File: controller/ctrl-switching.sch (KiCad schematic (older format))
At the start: 42 parts, among them J25 INDICATION1, J26 INDICATION2, U10 ULN2803A, U11 ULN2803A, U9 74HC595

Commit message: Change gas pedal interface so that it supports going up and down from the middle voltage so that it's compatible with Linde forklift gas mechanism
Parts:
- D35, D36, D37, D38, D39, D40, D41, D42, D43, D44, D45, D46, D47, D48, D49, D50: footprint (none) -> LEDs:LED_0805
- R23, R24, R25, R26, R27, R28, R29, R30, R31, R32, R33, R34, R35, R36, R37, R38, R39, R40, R41: footprint (none) -> Resistors_SMD:R_0603_HandSoldering
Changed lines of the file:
@@
 GAZ_SPEED1
 $Comp
-L GND #PWR013
+L GND #PWR18
 U 1 1 58CDDCEF
 P 7850 4800
-F 0 "#PWR013" H 4700 1700 50  0001 C CNN
+F 0 "#PWR18" H 4700 1700 50  0001 C CNN
 F 1 "GND" H 7855 4627 50  0000 C CNN
 F 2 "" H 4700 1950 50  0001 C CNN
@@
 $EndComp
 $Comp
-L GND #PWR014
+L GND #PWR19
 U 1 1 58CDDD09
 P 7950 9350
-F 0 "#PWR014" H 4800 6250 50  0001 C CNN
+F 0 "#PWR19" H 4800 6250 50  0001 C CNN
 F 1 "GND" H 7955 9177 50  0000 C CNN
 F 2 "" H 4800 6500 50  0001 C CNN
@@
 $EndComp
 $Comp
-L GND #PWR015
+L GND #PWR17
 U 1 1 58CDDF2F
 P 7400 9850
-F 0 "#PWR015" H 4250 6750 50  0001 C CNN
+F 0 "#PWR17" H 4250 6750 50  0001 C CNN
 F 1 "GND" H 7405 9677 50  0000 C CNN
 F 2 "" H 4250 7000 50  0001 C CNN
@@
 $EndComp
 $Comp
-L GND #PWR016
+L GND #PWR16
 U 1 1 58CDE24D
 P 7250 5300
-F 0 "#PWR016" H 4100 2200 50  0001 C CNN
+F 0 "#PWR16" H 4100 2200 50  0001 C CNN
 F 1 "GND" H 7255 5127 50  0000 C CNN
 F 2 "" H 4100 2450 50  0001 C CNN
@@
 DATA
 $Comp
-L +5V #PWR017
+L +5V #PWR14
 U 1 1 58CF6852
 P 4950 8050
-F 0 "#PWR017" H 1550 3750 50  0001 C CNN
+F 0 "#PWR14" H 1550 3750 50  0001 C CNN
 F 1 "+5V" H 4965 8223 50  0000 C CNN
 F 2 "" H 1550 3900 50  0001 C CNN
@@
 $EndComp
 $Comp
-L GND #PWR018
+L GND #PWR15
 U 1 1 58CF68A7
 P 5100 8950
-F 0 "#PWR018" H 1950 5850 50  0001 C CNN
+F 0 "#PWR15" H 1950 5850 50  0001 C CNN
 F 1 "GND" H 5105 8777 50  0000 C CNN
 F 2 "" H 1950 6100 50  0001 C CNN
@@
 F 0 "R23" V 4343 8350 50  0000 C CNN
 F 1 "R" V 4434 8350 50  0000 C CNN
-F 2 "" V 1730 4150 50  0001 C CNN
+F 2 "Resistors_SMD:R_0603_HandSoldering" V 1730 4150 50  0001 C CNN
 F 3 "" H 1800 4150 50  0001 C CNN
 	1    4550 8350
@@
 F 0 "R24" V 4343 8550 50  0000 C CNN
 F 1 "R" V 4434 8550 50  0000 C CNN
-F 2 "" V 1730 4350 50  0001 C CNN
+F 2 "Resistors_SMD:R_0603_HandSoldering" V 1730 4350 50  0001 C CNN
 F 3 "" H 1800 4350 50  0001 C CNN
 	1    4550 8550
@@
 F 0 "R25" V 4343 8850 50  0000 C CNN
 F 1 "R" V 4434 8850 50  0000 C CNN
-F 2 "" V 1730 4650 50  0001 C CNN
+F 2 "Resistors_SMD:R_0603_HandSoldering" V 1730 4650 50  0001 C CNN
 F 3 "" H 1800 4650 50  0001 C CNN
 	1    4550 8850
@@
 F 0 "D39" H 9400 2900 50  0000 C CNN
 F 1 "LED_Small_ALT" H 9400 2944 50  0001 C CNN
-F 2 "" V 1250 1700 50  0001 C CNN
+F 2 "LEDs:LED_0805" V 1250 1700 50  0001 C CNN
 F 3 "" V 1250 1700 50  0001 C CNN
 	1    9400 2800
@@
 F 0 "R30" V 9550 2800 50  0000 C CNN
 F 1 "R" V 9650 2800 50  0000 C CNN
-F 2 "" V 6830 -1400 50  0001 C CNN
+F 2 "Resistors_SMD:R_0603_HandSoldering" V 6830 -1400 50  0001 C CNN
 F 3 "" H 6900 -1400 50  0001 C CNN
 	1    9650 2800
@@
 F 0 "D40" H 9400 3100 50  0000 C CNN
 F 1 "LED_Small_ALT" H 9400 3144 50  0001 C CNN
-F 2 "" V 1250 1900 50  0001 C CNN
+F 2 "LEDs:LED_0805" V 1250 1900 50  0001 C CNN
 F 3 "" V 1250 1900 50  0001 C CNN
 	1    9400 3000
@@
 F 0 "R31" V 9550 3000 50  0000 C CNN
 F 1 "R" V 9650 3000 50  0000 C CNN
-F 2 "" V 6830 -1200 50  0001 C CNN
+F 2 "Resistors_SMD:R_0603_HandSoldering" V 6830 -1200 50  0001 C CNN
 F 3 "" H 6900 -1200 50  0001 C CNN
 	1    9650 3000
@@
 F 0 "D41" H 9400 3300 50  0000 C CNN
 F 1 "LED_Small_ALT" H 9400 3344 50  0001 C CNN
-F 2 "" V 1250 2100 50  0001 C CNN
+F 2 "LEDs:LED_0805" V 1250 2100 50  0001 C CNN
 F 3 "" V 1250 2100 50  0001 C CNN
 	1    9400 3200
@@
 F 0 "R32" V 9550 3200 50  0000 C CNN
 F 1 "R" V 9650 3200 50  0000 C CNN
-F 2 "" V 6830 -1000 50  0001 C CNN
+F 2 "Resistors_SMD:R_0603_HandSoldering" V 6830 -1000 50  0001 C CNN
 F 3 "" H 6900 -1000 50  0001 C CNN
 	1    9650 3200
@@
 F 0 "D42" H 9400 3500 50  0000 C CNN
 F 1 "LED_Small_ALT" H 9400 3544 50  0001 C CNN
-F 2 "" V 1250 2300 50  0001 C CNN
+F 2 "LEDs:LED_0805" V 1250 2300 50  0001 C CNN
 F 3 "" V 1250 2300 50  0001 C CNN
 	1    9400 3400
@@
 F 0 "R33" V 9550 3400 50  0000 C CNN
 F 1 "R" V 9650 3400 50  0000 C CNN
-F 2 "" V 6830 -800 50  0001 C CNN
+F 2 "Resistors_SMD:R_0603_HandSoldering" V 6830 -800 50  0001 C CNN
 F 3 "" H 6900 -800 50  0001 C CNN
 	1    9650 3400
@@
 F 0 "D35" H 9400 2100 50  0000 C CNN
 F 1 "LED_Small_ALT" H 9400 2144 50  0001 C CNN
-F 2 "" V 1250 900 50  0001 C CNN
+F 2 "LEDs:LED_0805" V 1250 900 50  0001 C CNN
 F 3 "" V 1250 900 50  0001 C CNN
 	1    9400 2000
@@
 F 0 "R26" V 9550 2000 50  0000 C CNN
 F 1 "R" V 9650 2000 50  0000 C CNN
-F 2 "" V 6830 -2200 50  0001 C CNN
+F 2 "Resistors_SMD:R_0603_HandSoldering" V 6830 -2200 50  0001 C CNN
 F 3 "" H 6900 -2200 50  0001 C CNN
 	1    9650 2000
@@
 F 0 "D36" H 9400 2300 50  0000 C CNN
 F 1 "LED_Small_ALT" H 9400 2344 50  0001 C CNN
-F 2 "" V 1250 1100 50  0001 C CNN
+F 2 "LEDs:LED_0805" V 1250 1100 50  0001 C CNN
 F 3 "" V 1250 1100 50  0001 C CNN
 	1    9400 2200
@@
 F 0 "R27" V 9550 2200 50  0000 C CNN
 F 1 "R" V 9650 2200 50  0000 C CNN
-F 2 "" V 6830 -2000 50  0001 C CNN
+F 2 "Resistors_SMD:R_0603_HandSoldering" V 6830 -2000 50  0001 C CNN
 F 3 "" H 6900 -2000 50  0001 C CNN
 	1    9650 2200
@@
 F 0 "D37" H 9400 2500 50  0000 C CNN
 F 1 "LED_Small_ALT" H 9400 2544 50  0001 C CNN
-F 2 "" V 1250 1300 50  0001 C CNN
+F 2 "LEDs:LED_0805" V 1250 1300 50  0001 C CNN
 F 3 "" V 1250 1300 50  0001 C CNN
 	1    9400 2400
@@
 F 0 "R28" V 9550 2400 50  0000 C CNN
 F 1 "R" V 9650 2400 50  0000 C CNN
-F 2 "" V 6830 -1800 50  0001 C CNN
+F 2 "Resistors_SMD:R_0603_HandSoldering" V 6830 -1800 50  0001 C CNN
 F 3 "" H 6900 -1800 50  0001 C CNN
 	1    9650 2400
@@
 F 0 "D38" H 9400 2700 50  0000 C CNN
 F 1 "LED_Small_ALT" H 9400 2744 50  0001 C CNN
-F 2 "" V 1250 1500 50  0001 C CNN
+F 2 "LEDs:LED_0805" V 1250 1500 50  0001 C CNN
 F 3 "" V 1250 1500 50  0001 C CNN
 	1    9400 2600
@@
 F 0 "R29" V 9550 2600 50  0000 C CNN
 F 1 "R" V 9650 2600 50  0000 C CNN
-F 2 "" V 6830 -1600 50  0001 C CNN
+F 2 "Resistors_SMD:R_0603_HandSoldering" V 6830 -1600 50  0001 C CNN
 F 3 "" H 6900 -1600 50  0001 C CNN
 	1    9650 2600
@@
 F 0 "D47" H 9500 7450 50  0000 C CNN
 F 1 "LED_Small_ALT" H 9500 7494 50  0001 C CNN
-F 2 "" V 1350 6250 50  0001 C CNN
+F 2 "LEDs:LED_0805" V 1350 6250 50  0001 C CNN
 F 3 "" V 1350 6250 50  0001 C CNN
 	1    9500 7350
@@
 F 0 "R38" V 9650 7350 50  0000 C CNN
 F 1 "R" V 9750 7350 50  0000 C CNN
-F 2 "" V 6930 3150 50  0001 C CNN
+F 2 "Resistors_SMD:R_0603_HandSoldering" V 6930 3150 50  0001 C CNN
 F 3 "" H 7000 3150 50  0001 C CNN
 	1    9750 7350
@@
 F 0 "D48" H 9500 7650 50  0000 C CNN
 F 1 "LED_Small_ALT" H 9500 7694 50  0001 C CNN
-F 2 "" V 1350 6450 50  0001 C CNN
+F 2 "LEDs:LED_0805" V 1350 6450 50  0001 C CNN
 F 3 "" V 1350 6450 50  0001 C CNN
 	1    9500 7550
@@
 F 0 "R39" V 9650 7550 50  0000 C CNN
 F 1 "R" V 9750 7550 50  0000 C CNN
-F 2 "" V 6930 3350 50  0001 C CNN
+F 2 "Resistors_SMD:R_0603_HandSoldering" V 6930 3350 50  0001 C CNN
 F 3 "" H 7000 3350 50  0001 C CNN
 	1    9750 7550
@@
 F 0 "D49" H 9500 7850 50  0000 C CNN
 F 1 "LED_Small_ALT" H 9500 7894 50  0001 C CNN
-F 2 "" V 1350 6650 50  0001 C CNN
+F 2 "LEDs:LED_0805" V 1350 6650 50  0001 C CNN
 F 3 "" V 1350 6650 50  0001 C CNN
 	1    9500 7750
@@
 F 0 "R40" V 9650 7750 50  0000 C CNN
 F 1 "R" V 9750 7750 50  0000 C CNN
-F 2 "" V 6930 3550 50  0001 C CNN
+F 2 "Resistors_SMD:R_0603_HandSoldering" V 6930 3550 50  0001 C CNN
 F 3 "" H 7000 3550 50  0001 C CNN
 	1    9750 7750
@@
 F 0 "D50" H 9500 8050 50  0000 C CNN
 F 1 "LED_Small_ALT" H 9500 8094 50  0001 C CNN
-F 2 "" V 1350 6850 50  0001 C CNN
+F 2 "LEDs:LED_0805" V 1350 6850 50  0001 C CNN
 F 3 "" V 1350 6850 50  0001 C CNN
 	1    9500 7950
@@
 F 0 "R41" V 9650 7950 50  0000 C CNN
 F 1 "R" V 9750 7950 50  0000 C CNN
-F 2 "" V 6930 3750 50  0001 C CNN
+F 2 "Resistors_SMD:R_0603_HandSoldering" V 6930 3750 50  0001 C CNN
 F 3 "" H 7000 3750 50  0001 C CNN
 	1    9750 7950
@@
 F 0 "D43" H 9500 6650 50  0000 C CNN
 F 1 "LED_Small_ALT" H 9500 6694 50  0001 C CNN
-F 2 "" V 1350 5450 50  0001 C CNN
+F 2 "LEDs:LED_0805" V 1350 5450 50  0001 C CNN
 F 3 "" V 1350 5450 50  0001 C CNN
 	1    9500 6550
@@
 F 0 "R34" V 9650 6550 50  0000 C CNN
 F 1 "R" V 9750 6550 50  0000 C CNN
-F 2 "" V 6930 2350 50  0001 C CNN
+F 2 "Resistors_SMD:R_0603_HandSoldering" V 6930 2350 50  0001 C CNN
 F 3 "" H 7000 2350 50  0001 C CNN
 	1    9750 6550
@@
 F 0 "D44" H 9500 6850 50  0000 C CNN
 F 1 "LED_Small_ALT" H 9500 6894 50  0001 C CNN
-F 2 "" V 1350 5650 50  0001 C CNN
+F 2 "LEDs:LED_0805" V 1350 5650 50  0001 C CNN
 F 3 "" V 1350 5650 50  0001 C CNN
 	1    9500 6750
@@
 F 0 "R35" V 9650 6750 50  0000 C CNN
 F 1 "R" V 9750 6750 50  0000 C CNN
-F 2 "" V 6930 2550 50  0001 C CNN
+F 2 "Resistors_SMD:R_0603_HandSoldering" V 6930 2550 50  0001 C CNN
 F 3 "" H 7000 2550 50  0001 C CNN
 	1    9750 6750
@@
 F 0 "D45" H 9500 7050 50  0000 C CNN
 F 1 "LED_Small_ALT" H 9500 7094 50  0001 C CNN
-F 2 "" V 1350 5850 50  0001 C CNN
+F 2 "LEDs:LED_0805" V 1350 5850 50  0001 C CNN
 F 3 "" V 1350 5850 50  0001 C CNN
 	1    9500 6950
@@
 F 0 "R36" V 9650 6950 50  0000 C CNN
 F 1 "R" V 9750 6950 50  0000 C CNN
-F 2 "" V 6930 2750 50  0001 C CNN
+F 2 "Resistors_SMD:R_0603_HandSoldering" V 6930 2750 50  0001 C CNN
 F 3 "" H 7000 2750 50  0001 C CNN
 	1    9750 6950
@@
 F 0 "D46" H 9500 7250 50  0000 C CNN
 F 1 "LED_Small_ALT" H 9500 7294 50  0001 C CNN
-F 2 "" V 1350 6050 50  0001 C CNN
+F 2 "LEDs:LED_0805" V 1350 6050 50  0001 C CNN
 F 3 "" V 1350 6050 50  0001 C CNN
 	1    9500 7150
@@
 F 0 "R37" V 9650 7150 50  0000 C CNN
 F 1 "R" V 9750 7150 50  0000 C CNN
-F 2 "" V 6930 2950 50  0001 C CNN
+F 2 "Resistors_SMD:R_0603_HandSoldering" V 6930 2950 50  0001 C CNN
 F 3 "" H 7000 2950 50  0001 C CNN
 	1    9750 7150

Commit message: More or less final controller board
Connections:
- net labels added: GAZ_SPEED3, ~GAZ_SPEED3_PWR

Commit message: Some progress with controller board routing
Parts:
- removed RN2: R_Network08, Resistors_THT:R_Array_SIP9, symbol R_Network08
- added RN2: R_Pack08, Resistors_SMD:R_Array_Convex_8x0602, symbol R_Pack08
- D35, D36, D37, D38, D39, D40, D41, D42, D45, D48, D49, D50: footprint LEDs:LED_0805 -> LEDs:LED_D5.0mm; Distributor (none) -> ?; Manufacturer (none) -> ?; PartNo (none) -> ?
- D43: renamed from D47; footprint LEDs:LED_0805 -> LEDs:LED_D5.0mm; Distributor (none) -> ?; Manufacturer (none) -> ?; PartNo (none) -> ?
- D44: renamed from D46; footprint LEDs:LED_0805 -> LEDs:LED_D5.0mm; Distributor (none) -> ?; Manufacturer (none) -> ?; PartNo (none) -> ?
- D46: renamed from D44; footprint LEDs:LED_0805 -> LEDs:LED_D5.0mm; Distributor (none) -> ?; Manufacturer (none) -> ?; PartNo (none) -> ?
- D47: renamed from D43; footprint LEDs:LED_0805 -> LEDs:LED_D5.0mm; Distributor (none) -> ?; Manufacturer (none) -> ?; PartNo (none) -> ?
- U9: footprint (none) -> Housings_SOIC:SOIC-16_3.9x9.9mm_Pitch1.27mm; Distributor (none) -> ?; Manufacturer (none) -> ?; PartNo (none) -> ?
- renumbered R38 to R34, R37 to R35, R35 to R37, R34 to R38
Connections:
- wire segments 96 -> 97

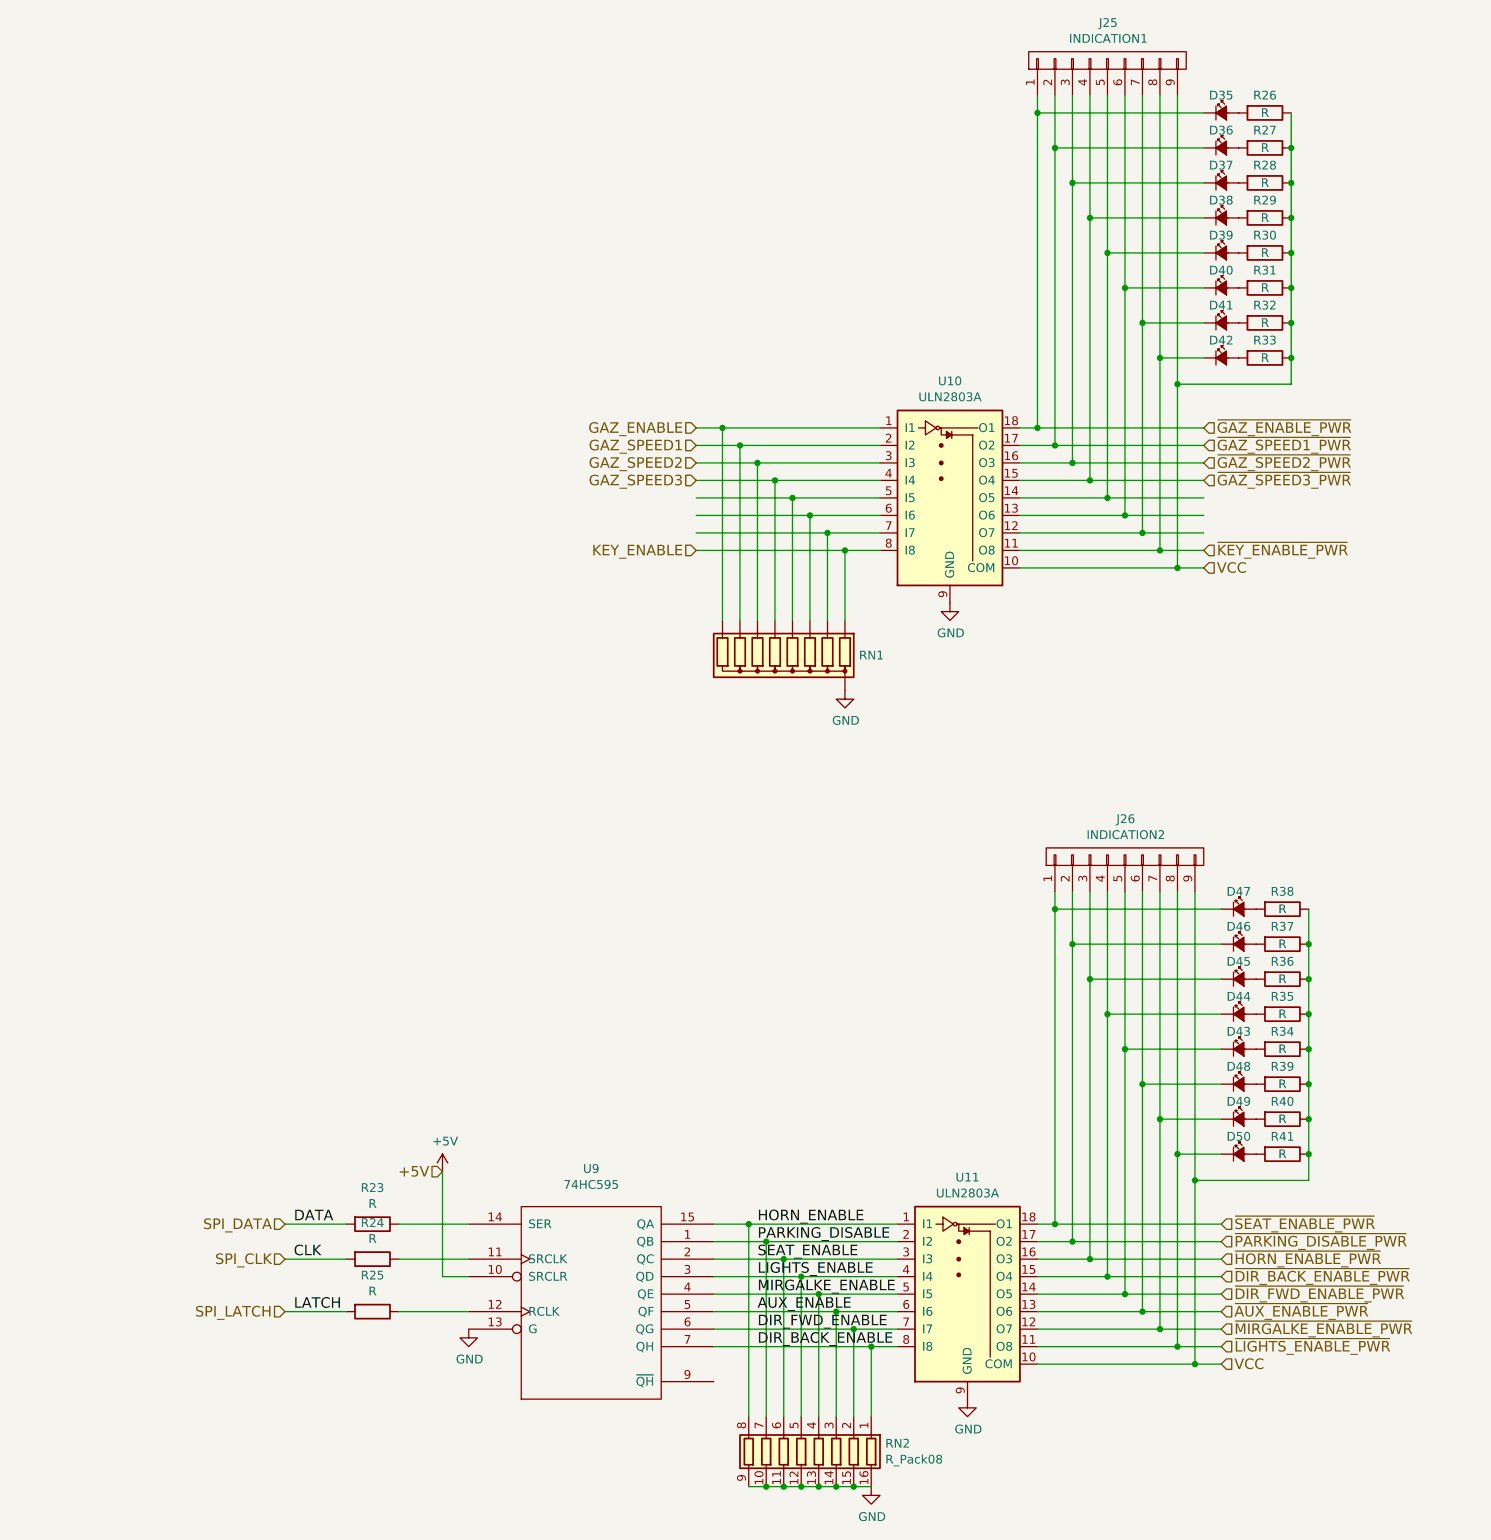
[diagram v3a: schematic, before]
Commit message: Finish the routing, add some significant fixes: *correct to-252 pin numbering * longer pads for relays * fix footprint of the optocouplers
Also finish the routing
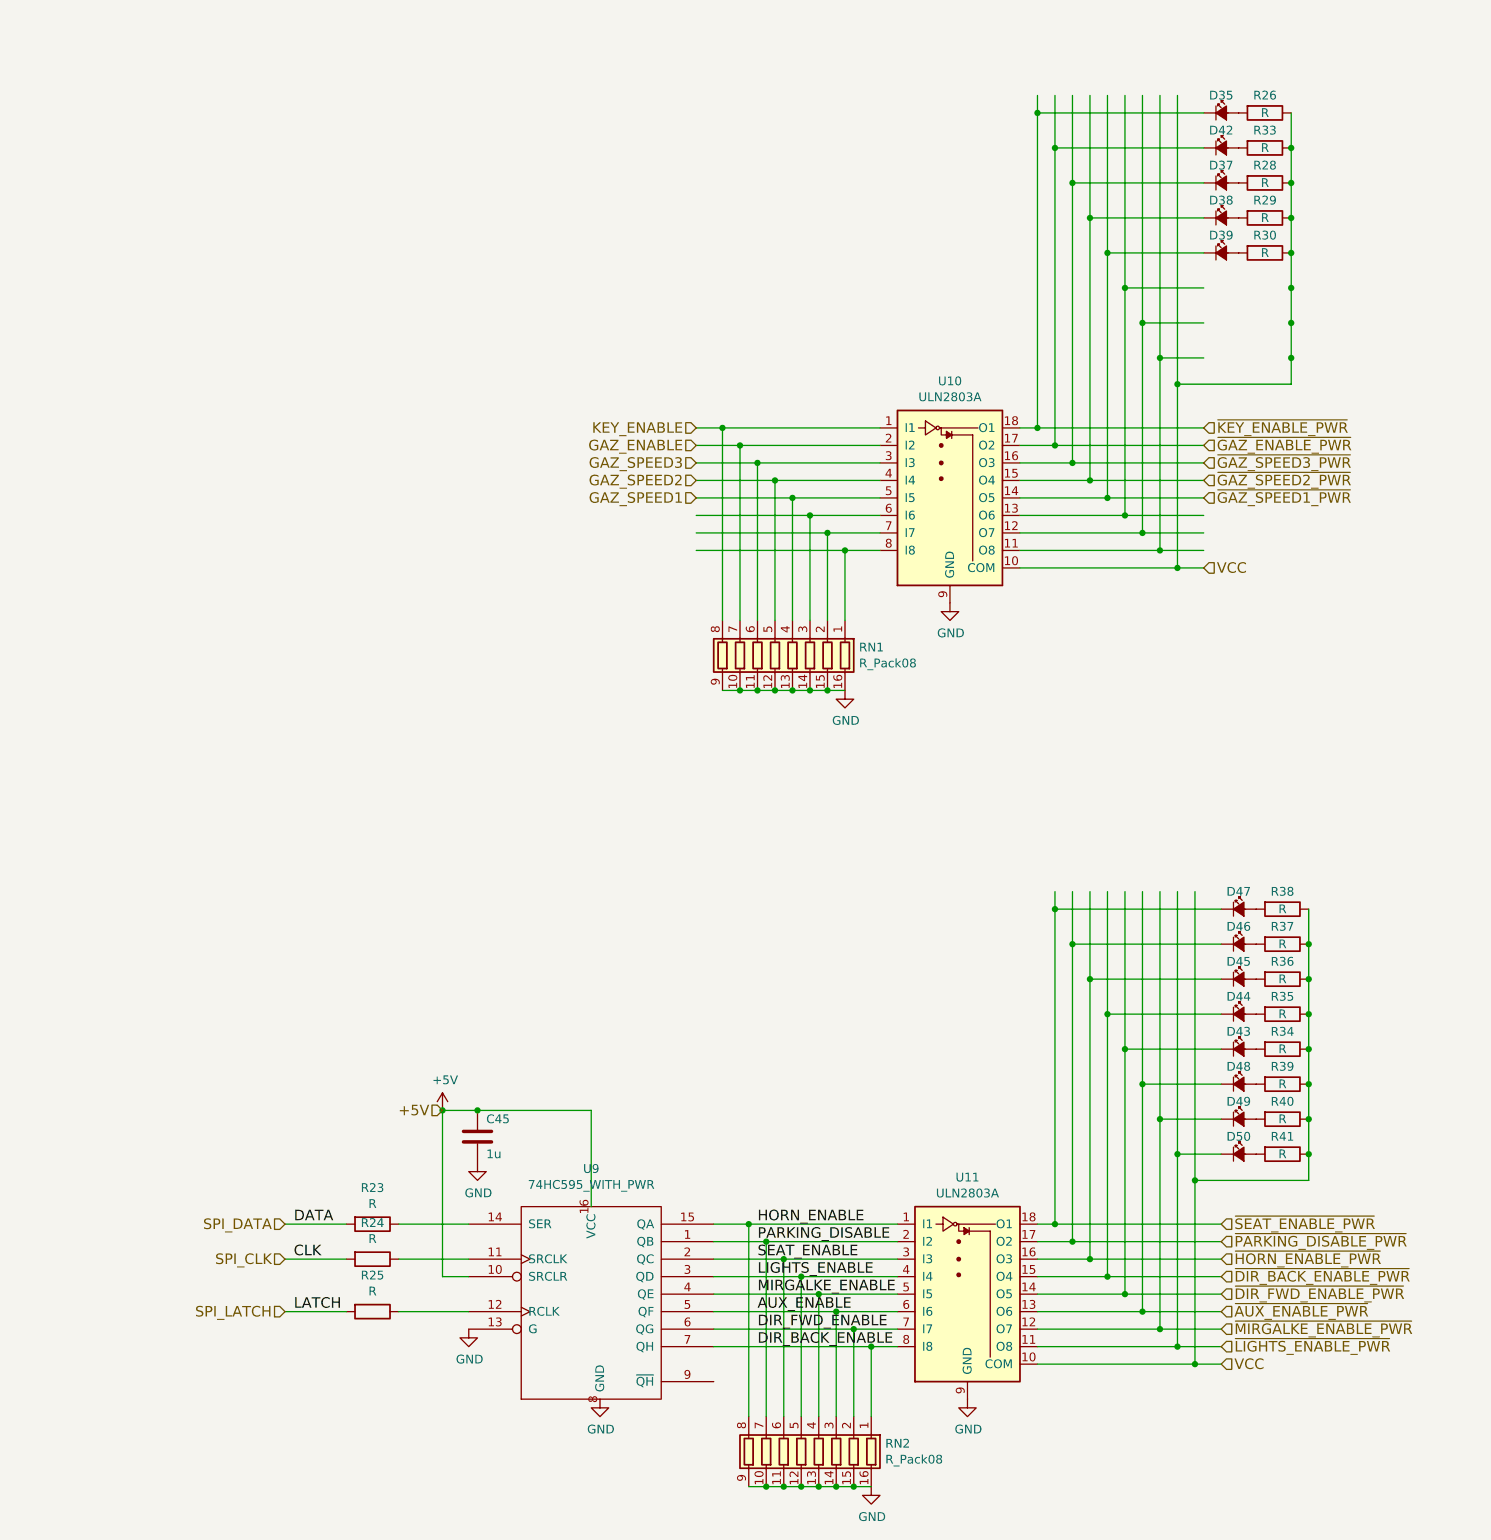
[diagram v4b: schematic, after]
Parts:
- removed D36, D40, D41: LED_Small_ALT, LEDs:LED_D5.0mm, symbol LED_Small_ALT
- removed J25: INDICATION1, symbol CONN_01X09
- removed J26: INDICATION2, symbol CONN_01X09
- removed R27, R31, R32: R, Resistors_SMD:R_0603_HandSoldering, symbol R
- removed RN1: R_Network08, Resistors_THT:R_Array_SIP9, symbol R_Network08
- removed U9: 74HC595, Housings_SOIC:SOIC-16_3.9x9.9mm_Pitch1.27mm, symbol 74HC595
- added C45: 1u, Capacitors_SMD:C_0603_HandSoldering, symbol C
- added RN1: R_Pack08, Resistors_SMD:R_Array_Convex_8x0602, symbol R_Pack08
- added U9: 74HC595_WITH_PWR, Housings_SOIC:SOIC-16_3.9x9.9mm_Pitch1.27mm, symbol 74HC595_WITH_PWR
- RN2: Distributor ? -> 9236236
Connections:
- wire segments 97 -> 100
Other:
- moved on the sheet: D42, R33
